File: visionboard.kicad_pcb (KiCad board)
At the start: 2 copper layers, 1 part, among them U1 Hirose DF40C-100DS-0.4V

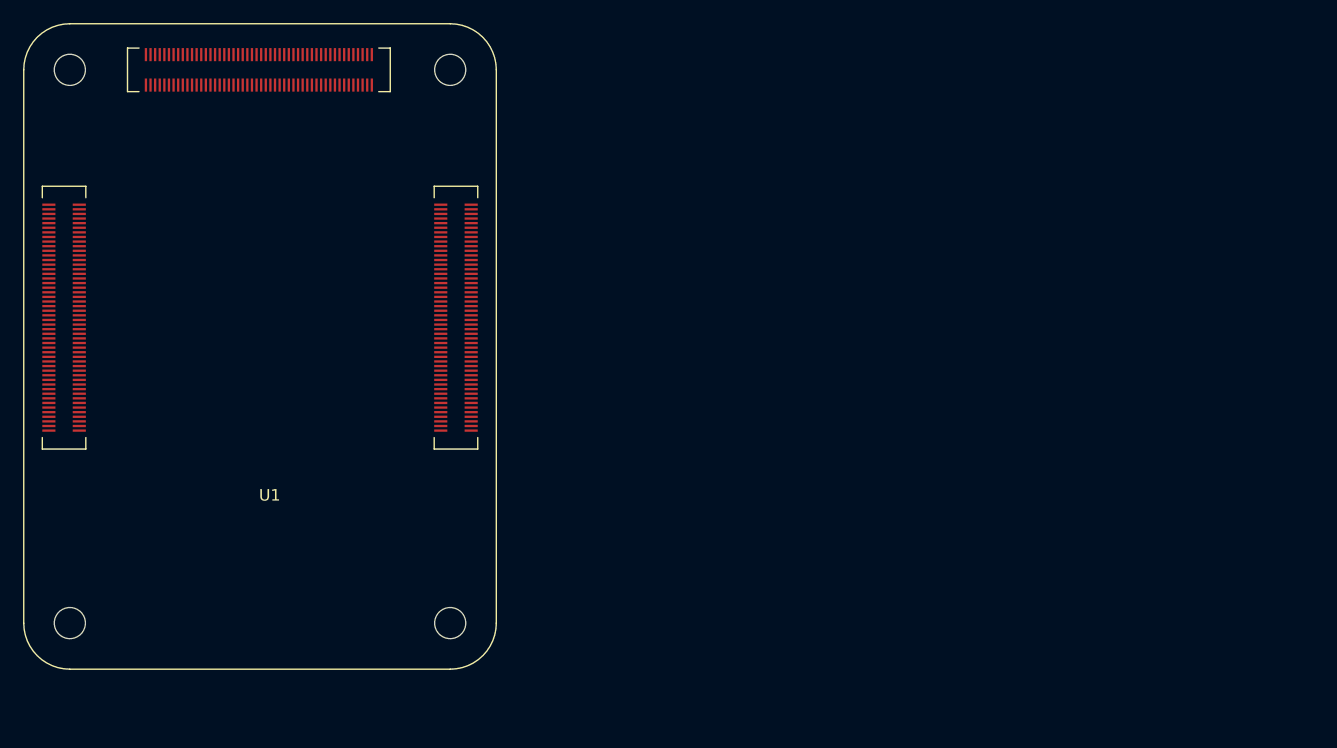
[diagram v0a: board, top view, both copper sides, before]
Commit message: Ethernet and MIPI cam done, USBC OTG started
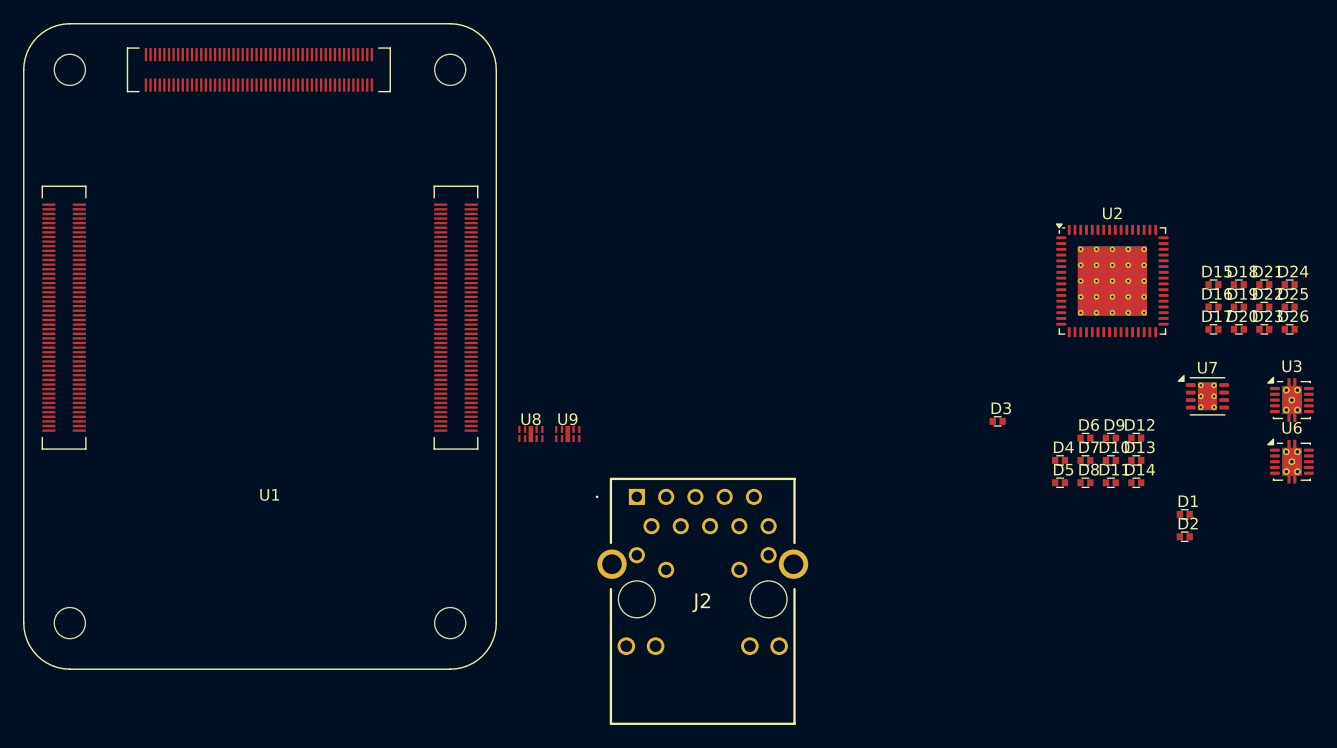
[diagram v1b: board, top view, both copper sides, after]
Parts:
- added D1: ESD5311N-2/TR, radxa:DFN1006-2L, F.Cu at (175.7, 86.1)
- added D10: ESD5311N-2/TR, radxa:DFN1006-2L, F.Cu at (169.3, 81.4)
- added D11: ESD5311N-2/TR, radxa:DFN1006-2L, F.Cu at (169.3, 83.3)
- added D12: ESD5311N-2/TR, radxa:DFN1006-2L, F.Cu at (171.5, 79.4)
- added D13: ESD5311N-2/TR, radxa:DFN1006-2L, F.Cu at (171.5, 81.4)
- added D14: ESD5311N-2/TR, radxa:DFN1006-2L, F.Cu at (171.5, 83.3)
- added D15: ESD5311N-2/TR, radxa:DFN1006-2L, F.Cu at (178.2, 66.1)
- added D16: ESD5311N-2/TR, radxa:DFN1006-2L, F.Cu at (178.2, 68.1)
- added D17: ESD5311N-2/TR, radxa:DFN1006-2L, F.Cu at (178.2, 70.0)
- added D18: ESD5311N-2/TR, radxa:DFN1006-2L, F.Cu at (180.4, 66.1)
- added D19: ESD5311N-2/TR, radxa:DFN1006-2L, F.Cu at (180.4, 68.1)
- added D2: ESD5311N-2/TR, radxa:DFN1006-2L, F.Cu at (175.7, 88.0)
- added D20: ESD5311N-2/TR, radxa:DFN1006-2L, F.Cu at (180.4, 70.0)
- added D21: ESD5311N-2/TR, radxa:DFN1006-2L, F.Cu at (182.6, 66.1)
- added D22: ESD5311N-2/TR, radxa:DFN1006-2L, F.Cu at (182.6, 68.1)
- added D23: ESD5311N-2/TR, radxa:DFN1006-2L, F.Cu at (182.6, 70.0)
- added D24: ESD5311N-2/TR, radxa:DFN1006-2L, F.Cu at (184.8, 66.1)
- added D25: ESD5311N-2/TR, radxa:DFN1006-2L, F.Cu at (184.8, 68.1)
- added D26: ESD5311N-2/TR, radxa:DFN1006-2L, F.Cu at (184.8, 70.0)
- added D3: ESD5311N-2/TR, radxa:DFN1006-2L, F.Cu at (159.5, 78.0)
- added D4: ESD5311N-2/TR, radxa:DFN1006-2L, F.Cu at (164.9, 81.4)
- added D5: ESD5311N-2/TR, radxa:DFN1006-2L, F.Cu at (164.9, 83.3)
- added D6: ESD5311N-2/TR, radxa:DFN1006-2L, F.Cu at (167.1, 79.4)
- added D7: ESD5311N-2/TR, radxa:DFN1006-2L, F.Cu at (167.1, 81.4)
- added D8: ESD5311N-2/TR, radxa:DFN1006-2L, F.Cu at (167.1, 83.3)
- added D9: ESD5311N-2/TR, radxa:DFN1006-2L, F.Cu at (169.3, 79.4)
- added J2: LPJG0926HENL, radxa:LPJG0926HENL, F.Cu at (128.2, 89.5)
- added U2: TUSB8041IPAPQ1, Package_DFN_QFN:QFN-64-1EP_9x9mm_P0.5mm_EP6x6mm_ThermalVias, F.Cu at (169.5, 70.8)
- added U3: TPS2561, Package_SON:VSON-10-1EP_3x3mm_P0.5mm_EP1.65x2.4mm_ThermalVias, F.Cu at (185.0, 81.2)
- added U6: TPS2561, Package_SON:VSON-10-1EP_3x3mm_P0.5mm_EP1.65x2.4mm_ThermalVias, F.Cu at (185.0, 86.5)
- added U7: TPS74611PQWDRBRQ1, Package_SON:VSON-8-1EP_3x3mm_P0.65mm_EP1.65x2.4mm_ThermalVias, F.Cu at (177.7, 80.8)
- added U8: ~, radxa:ESD5344-D, F.Cu at (119.0, 83.3)
- added U9: ~, radxa:ESD5344-D, F.Cu at (122.2, 83.3)
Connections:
- net GPIO19 renamed USBRST
- U1 pad 102: PCIe_CLK_nREQ -> unconnected-(U1B-PCIe_CLK_nREQ-Pad102)
- U1 pad 104: Reserved -> unconnected-(U1B-Reserved-Pad104)
- U1 pad 106: Reserved -> unconnected-(U1B-Reserved-Pad106)
- U1 pad 109: PCIe_nRST -> unconnected-(U1B-PCIe_nRST-Pad109)
- U1 pad 110: PCIe_CLK_P -> unconnected-(U1B-PCIe_CLK_P-Pad110)
- U1 pad 111: VDAC_COMP -> unconnected-(U1B-VDAC_COMP-Pad111)
- U1 pad 112: PCIe_CLK_N -> unconnected-(U1B-PCIe_CLK_N-Pad112)
- U1 pad 115: CAM1_D0_N -> unconnected-(U1B-CAM1_D0_N-Pad115)
- U1 pad 116: PCIe_RX_P -> unconnected-(U1B-PCIe_RX_P-Pad116)
- U1 pad 117: CAM1_D0_P -> unconnected-(U1B-CAM1_D0_P-Pad117)
- U1 pad 118: PCIe_RX_N -> unconnected-(U1B-PCIe_RX_N-Pad118)
- U1 pad 121: CAM1_D1_N -> unconnected-(U1B-CAM1_D1_N-Pad121)
- U1 pad 122: PCIe_TX_P -> unconnected-(U1B-PCIe_TX_P-Pad122)
- U1 pad 123: CAM1_D1_P -> unconnected-(U1B-CAM1_D1_P-Pad123)
- U1 pad 124: PCIe_TX_N -> unconnected-(U1B-PCIe_TX_N-Pad124)
- U1 pad 127: CAM1_C_N -> unconnected-(U1B-CAM1_C_N-Pad127)
- U1 pad 129: CAM1_C_P -> unconnected-(U1B-CAM1_C_P-Pad129)
- U1 pad 133: CAM1_D2_N -> unconnected-(U1B-CAM1_D2_N-Pad133)
- U1 pad 135: CAM1_D2_P -> unconnected-(U1B-CAM1_D2_P-Pad135)
- U1 pad 139: CAM1_D3_N -> unconnected-(U1B-CAM1_D3_N-Pad139)
- U1 pad 141: CAM1_D3_P -> unconnected-(U1B-CAM1_D3_P-Pad141)
- U1 pad 143: HDMI1_HOTPLUG -> unconnected-(U1B-HDMI1_HOTPLUG-Pad143)
- U1 pad 145: HDMI1_SDA -> unconnected-(U1B-HDMI1_SDA-Pad145)
- U1 pad 146: HDMI1_TX2_P -> unconnected-(U1B-HDMI1_TX2_P-Pad146)
- U1 pad 147: HDMI1_SCL -> unconnected-(U1B-HDMI1_SCL-Pad147)
- U1 pad 148: HDMI1_TX2_N -> unconnected-(U1B-HDMI1_TX2_N-Pad148)
- U1 pad 149: HDMI1_CEC -> unconnected-(U1B-HDMI1_CEC-Pad149)
- U1 pad 151: HDMI0_CEC -> unconnected-(U1B-HDMI0_CEC-Pad151)
- U1 pad 152: HDMI1_TX1_P -> unconnected-(U1B-HDMI1_TX1_P-Pad152)
- U1 pad 153: HDMI0_HOTPLUG -> unconnected-(U1B-HDMI0_HOTPLUG-Pad153)
- U1 pad 154: HDMI1_TX1_N -> unconnected-(U1B-HDMI1_TX1_N-Pad154)
- U1 pad 157: DSI0_D0_N -> unconnected-(U1B-DSI0_D0_N-Pad157)
- U1 pad 158: HDMI1_TX0_P -> unconnected-(U1B-HDMI1_TX0_P-Pad158)
- U1 pad 159: DSI0_D0_P -> unconnected-(U1B-DSI0_D0_P-Pad159)
- U1 pad 16: Ethernet_SYNC_IN(1.8v) -> unconnected-(U1A-Ethernet_SYNC_IN(1.8v)-Pad16)
- U1 pad 160: HDMI1_TX0_N -> unconnected-(U1B-HDMI1_TX0_N-Pad160)
- U1 pad 163: DSI0_D1_N -> unconnected-(U1B-DSI0_D1_N-Pad163)
- U1 pad 164: HDMI1_CLK_P -> unconnected-(U1B-HDMI1_CLK_P-Pad164)
- U1 pad 165: DSI0_D1_P -> unconnected-(U1B-DSI0_D1_P-Pad165)
- U1 pad 166: HDMI1_CLK_N -> unconnected-(U1B-HDMI1_CLK_N-Pad166)
- U1 pad 169: DSI0_C_N -> unconnected-(U1B-DSI0_C_N-Pad169)
- U1 pad 170: HDMI0_TX2_P -> unconnected-(U1B-HDMI0_TX2_P-Pad170)
- U1 pad 171: DSI0_C_P -> unconnected-(U1B-DSI0_C_P-Pad171)
- U1 pad 172: HDMI0_TX2_N -> unconnected-(U1B-HDMI0_TX2_N-Pad172)
- U1 pad 175: DSI1_D0_N -> unconnected-(U1B-DSI1_D0_N-Pad175)
- U1 pad 176: HDMI0_TX1_P -> unconnected-(U1B-HDMI0_TX1_P-Pad176)
- U1 pad 177: DSI1_D0_P -> unconnected-(U1B-DSI1_D0_P-Pad177)
- U1 pad 178: HDMI0_TX1_N -> unconnected-(U1B-HDMI0_TX1_N-Pad178)
- U1 pad 18: Ethernet_SYNC_OUT(1.8v) -> unconnected-(U1A-Ethernet_SYNC_OUT(1.8v)-Pad18)
- U1 pad 181: DSI1_D1_N -> unconnected-(U1B-DSI1_D1_N-Pad181)
- U1 pad 182: HDMI0_TX0_P -> unconnected-(U1B-HDMI0_TX0_P-Pad182)
- U1 pad 183: DSI1_D1_P -> unconnected-(U1B-DSI1_D1_P-Pad183)
- U1 pad 184: HDMI0_TX0_N -> unconnected-(U1B-HDMI0_TX0_N-Pad184)
- U1 pad 187: DSI1_C_N -> unconnected-(U1B-DSI1_C_N-Pad187)
- U1 pad 188: HDMI0_CLK_P -> unconnected-(U1B-HDMI0_CLK_P-Pad188)
- U1 pad 189: DSI1_C_P -> unconnected-(U1B-DSI1_C_P-Pad189)
- U1 pad 190: HDMI0_CLK_N -> unconnected-(U1B-HDMI0_CLK_N-Pad190)
- U1 pad 193: DSI1_D2_N -> unconnected-(U1B-DSI1_D2_N-Pad193)
- U1 pad 194: DSI1_D3_N -> unconnected-(U1B-DSI1_D3_N-Pad194)
- U1 pad 195: DSI1_D2_P -> unconnected-(U1B-DSI1_D2_P-Pad195)
- U1 pad 196: DSI1_D3_P -> unconnected-(U1B-DSI1_D3_P-Pad196)
- U1 pad 199: HDMI0_SDA -> unconnected-(U1B-HDMI0_SDA-Pad199)
- U1 pad 200: HDMI0_SCL -> unconnected-(U1B-HDMI0_SCL-Pad200)
- U1 pad 239: RSVD -> unconnected-(U1C-RSVD-Pad239)
- U1 pad 241: RSVD -> unconnected-(U1C-RSVD-Pad241)
- U1 pad 274: SDMMC_DET_L -> unconnected-(U1C-SDMMC_DET_L-Pad274)
- U1 pad 36: ID_SD -> unconnected-(U1A-ID_SD-Pad36)
- U1 pad 57: SD_CLK -> unconnected-(U1A-SD_CLK-Pad57)
- U1 pad 61: SD_DAT3 -> unconnected-(U1A-SD_DAT3-Pad61)
- U1 pad 62: SD_CMD -> unconnected-(U1A-SD_CMD-Pad62)
- U1 pad 63: SD_DAT0 -> unconnected-(U1A-SD_DAT0-Pad63)
- U1 pad 64: SD_DAT5 -> unconnected-(U1A-SD_DAT5-Pad64)
- U1 pad 67: SD_DAT1 -> unconnected-(U1A-SD_DAT1-Pad67)
- U1 pad 68: SD_DAT4 -> unconnected-(U1A-SD_DAT4-Pad68)
- U1 pad 69: SD_DAT2 -> unconnected-(U1A-SD_DAT2-Pad69)
- U1 pad 70: SD_DAT7 -> unconnected-(U1A-SD_DAT7-Pad70)
- U1 pad 72: SD_DAT6 -> unconnected-(U1A-SD_DAT6-Pad72)
- U1 pad 73: SD_VDD_Override -> unconnected-(U1A-SD_VDD_Override-Pad73)
- U1 pad 75: SD_PWR_ON -> unconnected-(U1A-SD_PWR_ON-Pad75)
- U1 pad 76: Reserved -> unconnected-(U1A-Reserved-Pad76)
- U1 pad 78: GPIO_VREF(1.8v/3.3v_Input) -> unconnected-(U1A-GPIO_VREF(1.8v/3.3v_Input)-Pad78)
